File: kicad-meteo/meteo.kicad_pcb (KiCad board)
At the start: 2 copper layers, 38.4 x 62.7 mm, 17 parts, among them J1 BUCK, J2 Connector I2C extension, J3 Solar_Panel, J4 Battery, J5 Battery_Internal, SW1 SW_DIP_x01, U1 DHT11, U2 DS18B20, U4 MOUDLE-SEEEDUINO-XIAO-ESP32C3

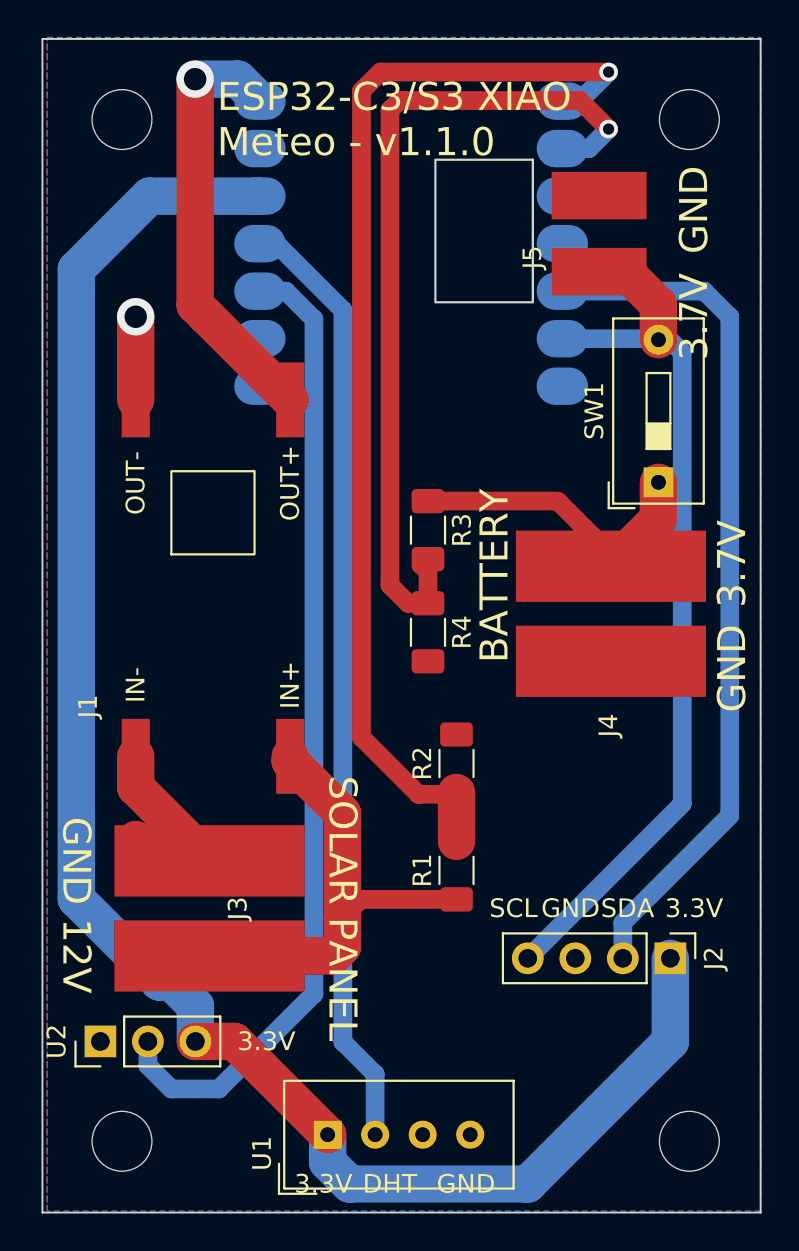
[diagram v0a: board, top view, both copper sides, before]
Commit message: feat(meteo): fix pin mapping and add switch, v1.1.0
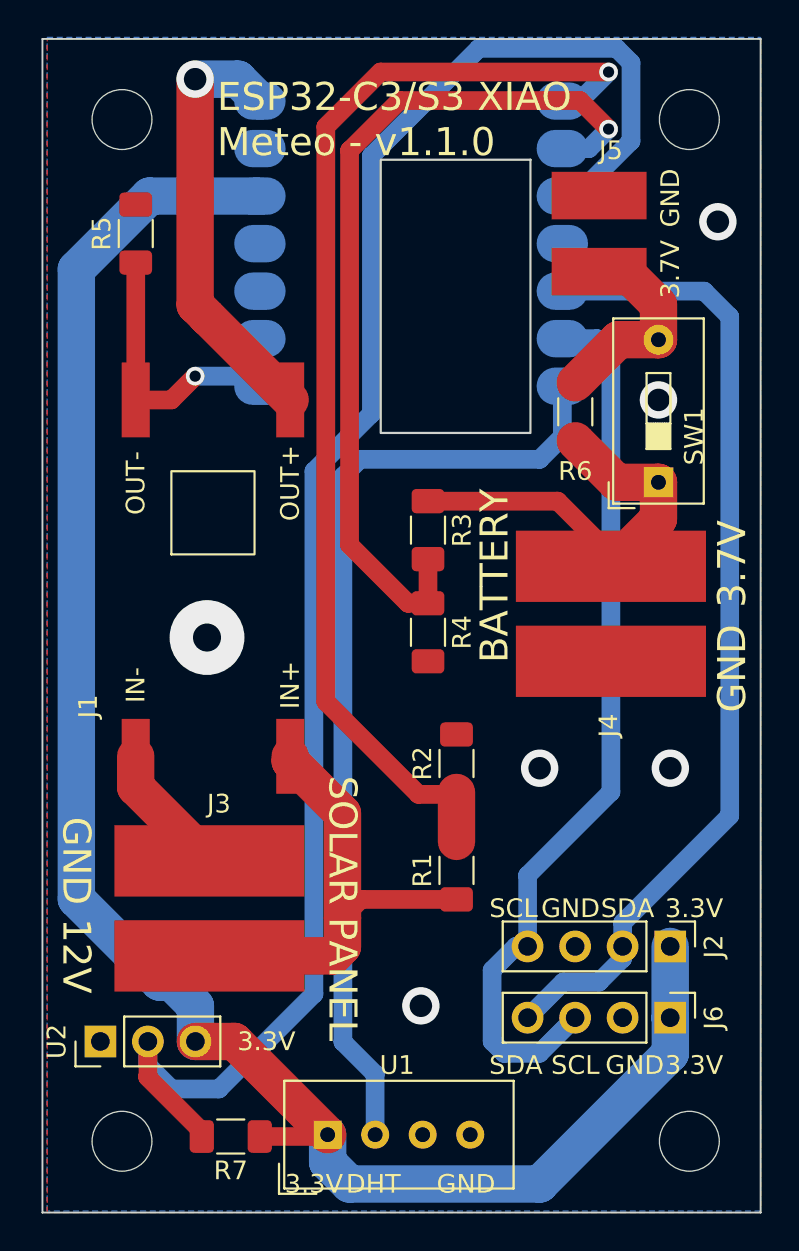
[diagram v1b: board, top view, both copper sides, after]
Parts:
- added J6: Connector I2C extension, Connector_PinHeader_2.54mm:PinHeader_1x04_P2.54mm_Vertical, F.Cu at (227.3, 82.5)
- added R5: 0.1, Resistor_SMD:R_1206_3216Metric_Pad1.30x1.75mm_HandSolder, F.Cu at (198.8, 40.6)
- added R6: R, Resistor_SMD:R_1206_3216Metric_Pad1.30x1.75mm_HandSolder, F.Cu at (222.2, 50.2)
- added R7: 4.7k, Resistor_SMD:R_1206_3216Metric_Pad1.30x1.75mm_HandSolder, F.Cu at (203.8, 88.9)
- R1: value R -> 180k
- R2: value R -> 20k
- R3, R4: value R -> 100k
- moved J2 0.64 mm to (227.3, 78.7)
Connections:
- net PROBE_BATT renamed PROBE_BATT_V
- J1 pad 4: GND -> PROBE_BATT_I
- U4 pad 10: ONE_WIRE -> unconnected-(U4-Pad10)
- U4 pad 11: DHT -> unconnected-(U4-Pad11)
- U4 pad 3: unconnected-(U4-Pad3) -> ONE_WIRE
- U4 pad 7: unconnected-(U4-Pad7) -> DHT
- U4 pad 8: unconnected-(U4-Pad8) -> PROBE_BATT_I
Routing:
- net SCL: track 0.00 -> 48.2 mm
- net ONE_WIRE: track 52.4 -> 90.8 mm
- net +BATT: track 48.3 -> 11.2 mm
- net PROBE_BATT_I: track 0.00 -> 14.7 mm, vias 0 -> 1
- net SDA: track 46.2 -> 52.6 mm
- net +3.3V: track 92.7 -> 97.4 mm
- net GND: track 4.45 -> 0.00 mm, vias 1 -> 6
- net +12V: track 29.6 -> 25.1 mm
- net Net-(J4-Pad1): track 18.0 -> 21.9 mm
- net GNDPWR: track 9.01 -> 7.22 mm
- net PROBE_SOLAR: track 60.3 -> 61.9 mm
- net PROBE_BATT_V: track 46.1 -> 47.4 mm

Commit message: fix: add pull-up for DHT-22
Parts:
- added R8: 4.7k, Resistor_SMD:R_1206_3216Metric_Pad1.30x1.75mm_HandSolder, F.Cu at (213.4, 84.5)
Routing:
- net DHT: track 51.2 -> 57.7 mm
- net +3.3V: track 97.4 -> 103.1 mm
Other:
- board text added: "ESP32-C3/S3 XIAO Meteo - v1.1.1"
- board text removed: "ESP32-C3/S3 XIAO Meteo - v1.1.0"
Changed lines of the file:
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@@
+    )
+  )
+  (footprint "Resistor_SMD:R_1206_3216Metric_Pad1.30x1.75mm_HandSolder" (layer "F.Cu")
+    (at 213.36 84.455)
+    (descr "Resistor SMD 1206 (3216 Metric), square (rectangular) end terminal, IPC_7351 nominal with elongated pad for handsoldering. (Body size source: IPC-SM-782 page 72, https://www.pcb-3d.com/wordpress/wp-content/uploads/ipc-sm-782a_amendment_1_and_2.pdf), generated with kicad-footprint-generator")
+    (tags "resistor handsolder")
+    (property "Sheetfile" "meteo.kicad_sch")
+    (property "Sheetname" "")
+    (attr smd)
+    (fp_text reference "R8" (at 0 -1.82) (layer "F.SilkS")
+      (effects (font (size 1 1) (thickness 0.15)))
+    )
+    (fp_text value "4.7k" (at 0 1.82) (layer "F.Fab")
+      (effects (font (size 1 1) (thickness 0.15)))
+    )
+    (fp_text user "${REFERENCE}" (at 0 0) (layer "F.Fab")
+      (effects (font (size 0.8 0.8) (thickness 0.12)))
+    )
+    (fp_line (start -0.727064 0.91) (end 0.727064 0.91) (layer "F.SilkS") (width 0.12))
+    (fp_line (start -0.727064 -0.91) (end 0.727064 -0.91) (layer "F.SilkS") (width 0.12))
+    (fp_line (start -2.45 1.12) (end -2.45 -1.12) (layer "F.CrtYd") (width 0.05))
+    (fp_line (start 2.45 1.12) (end -2.45 1.12) (layer "F.CrtYd") (width 0.05))
+    (fp_line (start -2.45 -1.12) (end 2.45 -1.12) (layer "F.CrtYd") (width 0.05))
+    (fp_line (start 2.45 -1.12) (end 2.45 1.12) (layer "F.CrtYd") (width 0.05))
+    (fp_line (start 1.6 -0.8) (end 1.6 0.8) (layer "F.Fab") (width 0.1))
+    (fp_line (start 1.6 0.8) (end -1.6 0.8) (layer "F.Fab") (width 0.1))
+    (fp_line (start -1.6 0.8) (end -1.6 -0.8) (layer "F.Fab") (width 0.1))
+    (fp_line (start -1.6 -0.8) (end 1.6 -0.8) (layer "F.Fab") (width 0.1))
+    (pad "1" smd roundrect (at -1.55 0) (size 1.3 1.75) (layers "F.Cu" "F.Paste" "F.Mask") (roundrect_rratio 0.192308)
+      (net 4 "+3.3V") (pintype "passive"))
+    (pad "2" smd roundrect (at 1.55 0) (size 1.3 1.75) (layers "F.Cu" "F.Paste" "F.Mask") (roundrect_rratio 0.192308)
+      (net 5 "DHT") (pintype "passive"))
+    (model "${KICAD6_3DMODEL_DIR}/Resistor_SMD.3dshapes/R_1206_3216Metric.wrl"
+      (offset (xyz 0 0 0))
+      (scale (xyz 1 1 1))
+      (rotate (xyz 0 0 0))
     )
   )
@@
     (effects (font (size 1.5 1.5) (thickness 0.3)))
   )
-  (gr_text "ESP32-C3/S3 XIAO\nMeteo - v1.1.0" (at 203.101 34.544) (layer "F.SilkS")
+  (gr_text "ESP32-C3/S3 XIAO\nMeteo - v1.1.1" (at 203.101 34.544) (layer "F.SilkS")
     (effects (font (size 1.5 1.5) (thickness 0.3)) (justify left))
   )
@@
   (segment (start 226.695 44.45) (end 226.695 46.3125) (width 2) (layer "F.Cu") (net 3))
   (segment (start 204.03 83.82) (end 209.0125 88.8025) (width 2) (layer "F.Cu") (net 4))
+  (segment (start 211.81 84.455) (end 211.455 84.455) (width 1) (layer "F.Cu") (net 4))
   (segment (start 205.385 88.9) (end 208.915 88.9) (width 1) (layer "F.Cu") (net 4))
+  (segment (start 211.455 84.455) (end 209.0125 86.8975) (width 1) (layer "F.Cu") (net 4))
   (segment (start 201.945 83.82) (end 204.03 83.82) (width 2) (layer "F.Cu") (net 4))
+  (segment (start 209.0125 86.8975) (end 209.0125 88.8025) (width 1) (layer "F.Cu") (net 4))
   (segment (start 208.915 88.9) (end 209.0125 88.8025) (width 1) (layer "F.Cu") (net 4))
   (segment (start 200.025 80.645) (end 200.66 80.645) (width 2) (layer "B.Cu") (net 4))
@@
   (segment (start 199.488924 38.636076) (end 195.58 42.545) (width 2) (layer "B.Cu") (net 4))
   (segment (start 209.0125 90.2675) (end 210.185 91.44) (width 2) (layer "B.Cu") (net 4))
+  (segment (start 214.91 85.445) (end 213.36 86.995) (width 1) (layer "F.Cu") (net 5))
+  (segment (start 211.5525 87.5325) (end 211.5525 88.8025) (width 1) (layer "F.Cu") (net 5))
+  (segment (start 213.36 86.995) (end 212.09 86.995) (width 1) (layer "F.Cu") (net 5))
+  (segment (start 214.91 84.455) (end 214.91 85.445) (width 1) (layer "F.Cu") (net 5))
+  (segment (start 212.09 86.995) (end 211.5525 87.5325) (width 1) (layer "F.Cu") (net 5))
   (segment (start 220.345 52.705) (end 210.739 52.705) (width 1) (layer "B.Cu") (net 5))
   (segment (start 210.739 52.705) (end 209.827 53.617) (width 1) (layer "B.Cu") (net 5))

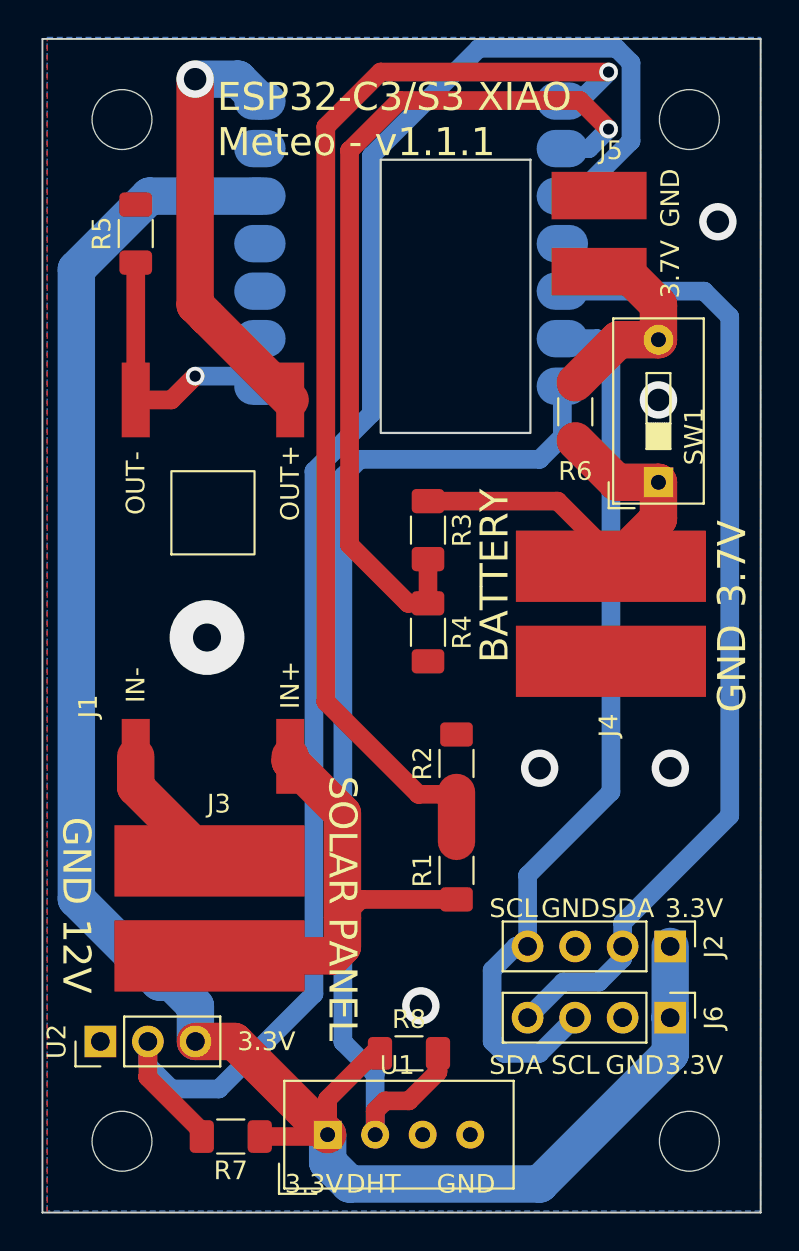
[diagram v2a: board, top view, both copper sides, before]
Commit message: fix: correct AD pin for monitoring and ground
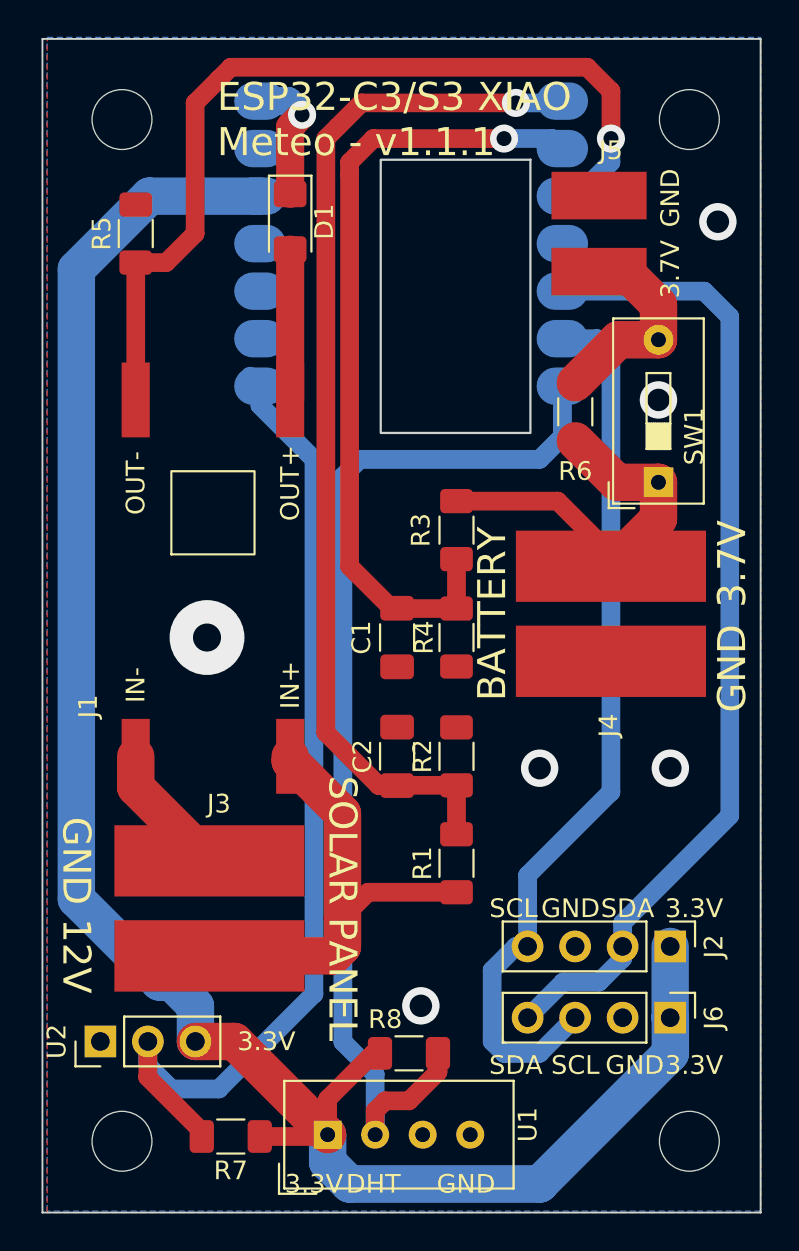
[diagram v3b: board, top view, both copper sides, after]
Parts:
- added C1: C, Capacitor_SMD:C_1206_3216Metric_Pad1.33x1.80mm_HandSolder, F.Cu at (212.7, 62.2)
- added C2: C, Capacitor_SMD:C_1206_3216Metric_Pad1.33x1.80mm_HandSolder, F.Cu at (212.7, 68.6)
- added D1: D_Schottky, Diode_SMD:D_1206_3216Metric_Pad1.42x1.75mm_HandSolder, F.Cu at (207.0, 40.0)
- moved R4 1.55 mm to (215.9, 62.2)
- moved R3 1.52 mm to (215.9, 56.5)
- moved R1 0.38 mm to (215.9, 74.3)
- moved R2 0.38 mm to (215.9, 68.6)
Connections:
- J1 pad 3: +5V -> Net-(J1-Pad3)
- U4 pad 3: ONE_WIRE -> PROBE_BATT_I
- U4 pad 8: PROBE_BATT_I -> ONE_WIRE
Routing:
- net ONE_WIRE: track 90.8 -> 53.5 mm
- net PROBE_BATT_I: track 14.7 -> 48.8 mm
- net +5V: track 23.2 -> 7.05 mm
- net Net-(J1-Pad3): track 0.00 -> 8.04 mm
- net PROBE_SOLAR: track 61.9 -> 56.0 mm
- net PROBE_BATT_V: track 47.4 -> 43.0 mm
- net Net-(J4-Pad1): track 21.9 -> 20.3 mm
